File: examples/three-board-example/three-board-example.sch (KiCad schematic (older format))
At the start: 3 parts, among them U1 LM555xM, U2 LM555xM

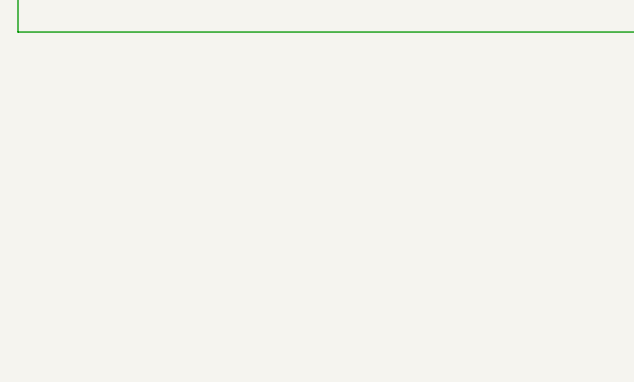
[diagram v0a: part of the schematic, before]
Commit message: Special modules for cutting, meaning that the drawings from within the modules are exploded to cut layers
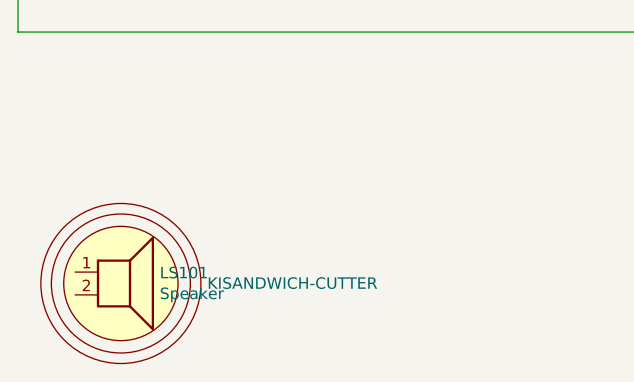
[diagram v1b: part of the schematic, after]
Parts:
- added KS101: KISANDWICH-CUTTER, Alex_Connectors:CUI-speaker-3layer-tight, symbol sandwich-features:Speaker-cutout-3board
- added LS101: Speaker, Alex_Connectors:Speaker_CUI_CLS0281MAE_embedded, symbol Device:Speaker
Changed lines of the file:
@@
+	1    0    0    -1
+$EndComp
+$Comp
+L Device:Speaker LS101
+U 1 1 6044355E
+P 4000 4850
+F 0 "LS101" H 4170 4846 50  0000 L CNN
+F 1 "Speaker" H 4170 4755 50  0000 L CNN
+F 2 "Alex_Connectors:Speaker_CUI_CLS0281MAE_embedded" H 4000 4650 50  0001 C CNN
+F 3 "~" H 3990 4800 50  0001 C CNN
+	1    4000 4850
+	1    0    0    -1
+$EndComp
+$Comp
+L sandwich-features:Speaker-cutout-3board KS101
+U 1 1 60443B6A
+P 4000 4900
+F 0 "KS101" H 4000 4900 50  0001 C CNN
+F 1 "KISANDWICH-CUTTER" H 4378 4900 50  0000 L CNN
+F 2 "Alex_Connectors:CUI-speaker-3layer-tight" H 4000 4900 50  0001 C CNN
+F 3 "" H 4000 4900 50  0001 C CNN
+	1    4000 4900
 	1    0    0    -1
 $EndComp

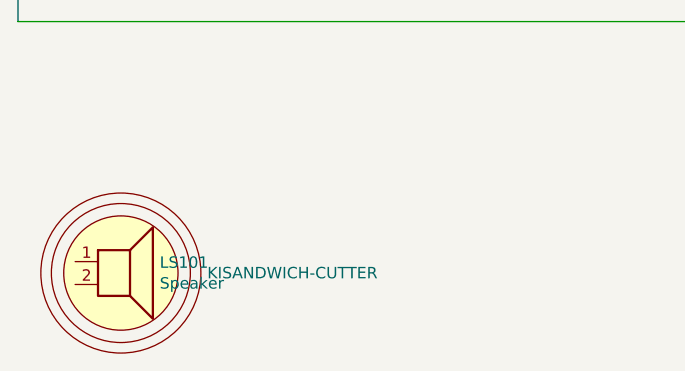
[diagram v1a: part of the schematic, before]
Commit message: Made 3D representations. Changed speaker to being placed on midboard. Checked heights
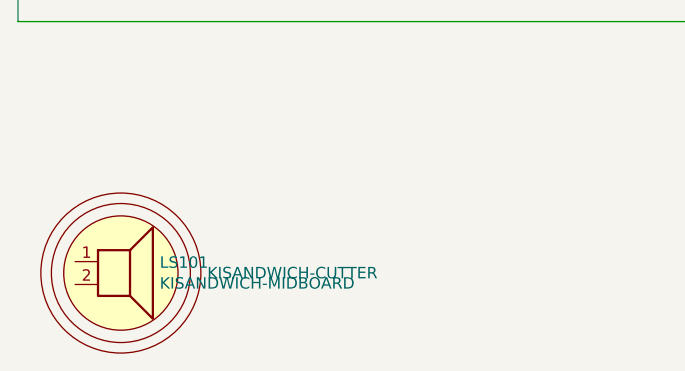
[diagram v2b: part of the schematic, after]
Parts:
- LS101: value Speaker -> KISANDWICH-MIDBOARD
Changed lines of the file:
@@
 P 4000 4850
 F 0 "LS101" H 4170 4846 50  0000 L CNN
-F 1 "Speaker" H 4170 4755 50  0000 L CNN
+F 1 "KISANDWICH-MIDBOARD" H 4170 4755 50  0000 L CNN
 F 2 "Alex_Connectors:Speaker_CUI_CLS0281MAE_embedded" H 4000 4650 50  0001 C CNN
 F 3 "~" H 3990 4800 50  0001 C CNN
